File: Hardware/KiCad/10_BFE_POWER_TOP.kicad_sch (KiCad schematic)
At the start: 0 parts

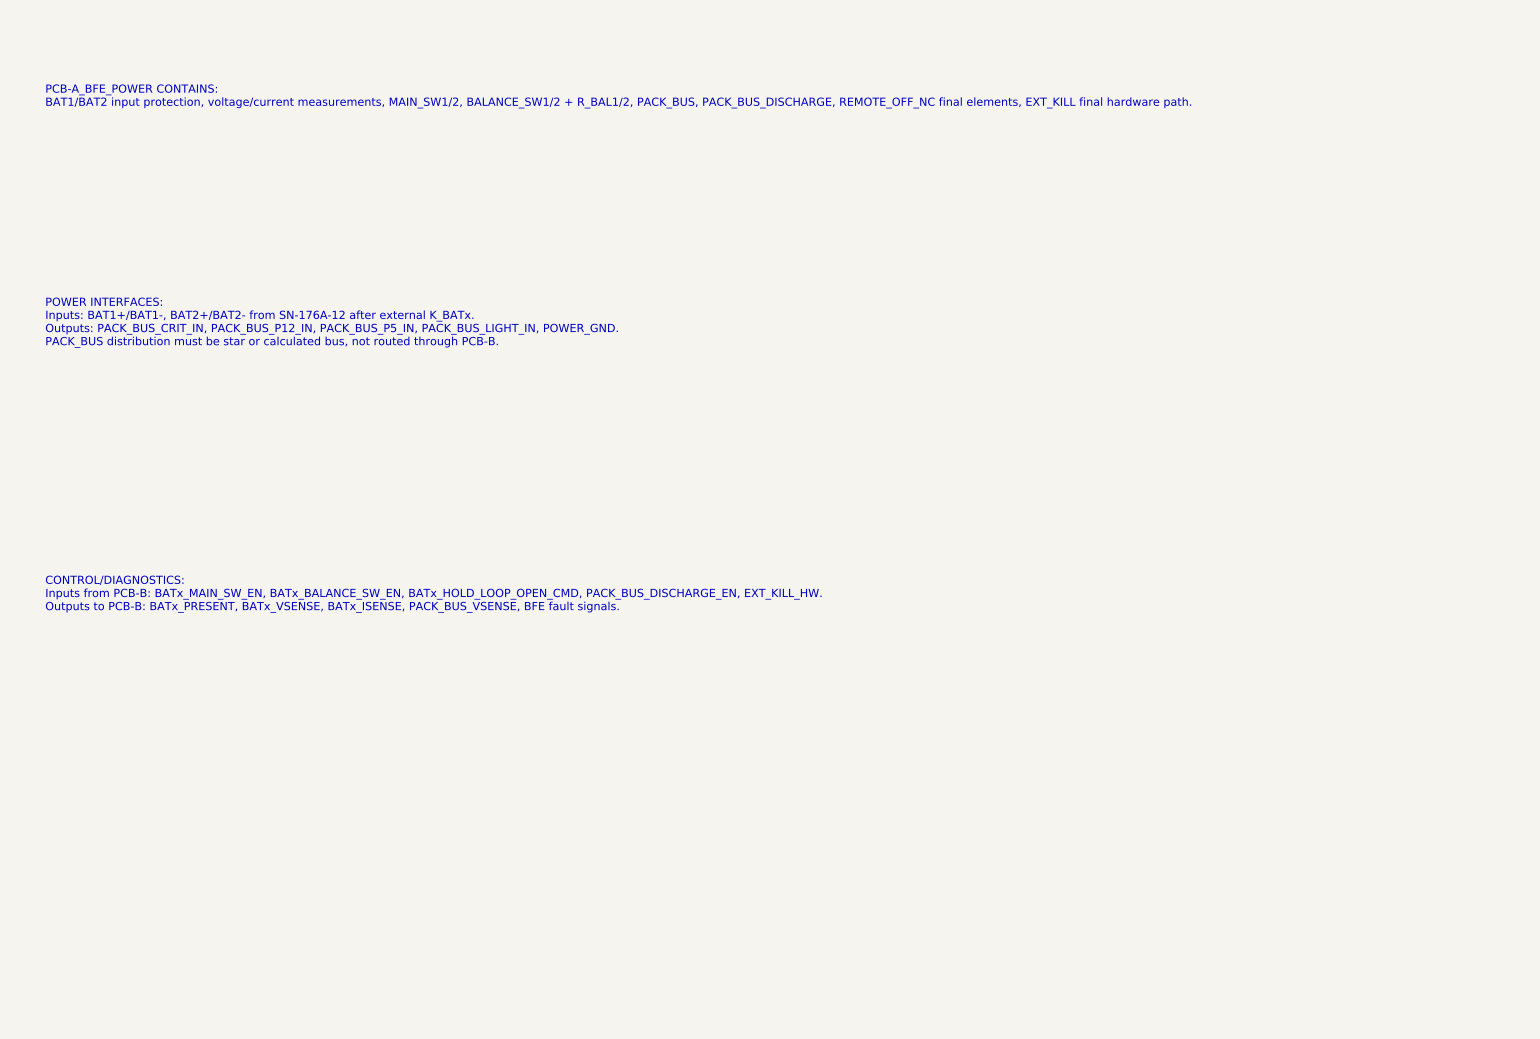
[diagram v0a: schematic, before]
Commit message: hardware: detail 10 BFE power top sheet
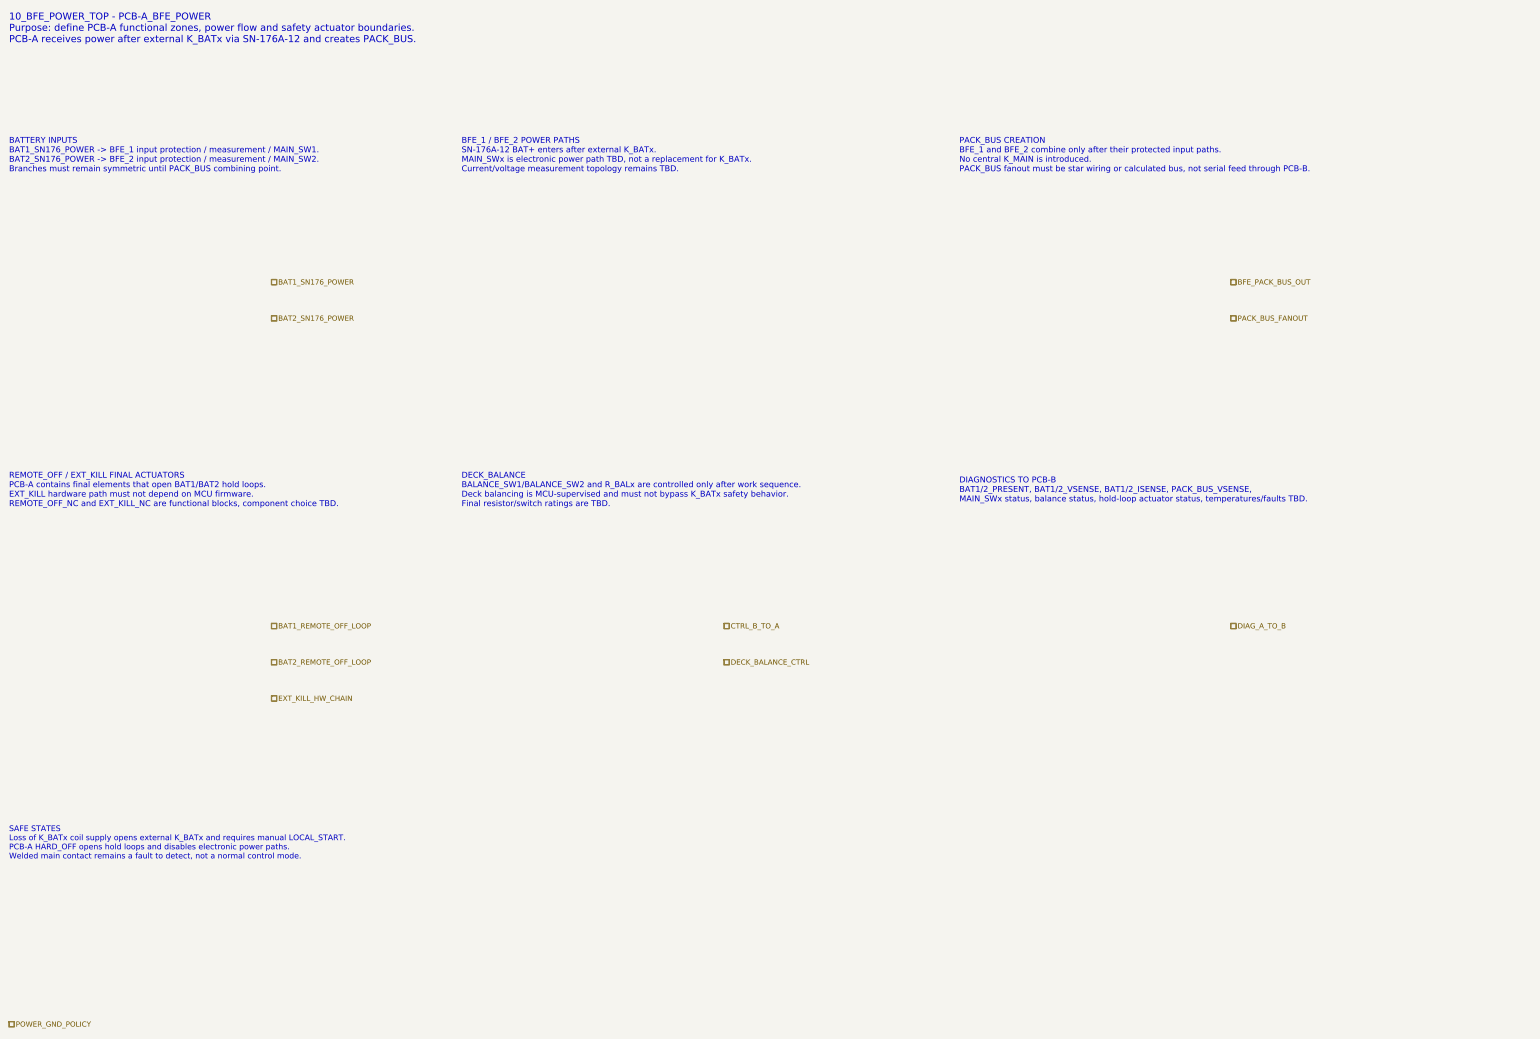
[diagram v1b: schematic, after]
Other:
- note added: "10_BFE_POWER_TOP - PCB-A_BFE_POWER Purpose: define PCB-A functional zones, power flow and safety actuator boundaries. PCB-A receives power after external K_BATx via SN-176A-12 and creates PACK_BUS."
- note added: "BATTERY INPUTS BAT1_SN176_POWER -> BFE_1 input protection / measurement / MAIN_SW1. BAT2_SN176_POWER -> BFE_2 input protection / measurement / MAIN_SW2. Branches must remain symmetric until PACK_BUS combining point."
- note added: "BFE_1 / BFE_2 POWER PATHS SN-176A-12 BAT+ enters after external K_BATx. MAIN_SWx is electronic power path TBD, not a replacement for K_BATx. Current/voltage measurement topology remains TBD."
- note added: "DECK_BALANCE BALANCE_SW1/BALANCE_SW2 and R_BALx are controlled only after work sequence. Deck balancing is MCU-supervised and must not bypass K_BATx safety behavior. Final resistor/switch ratings are TBD."
- note added: "DIAGNOSTICS TO PCB-B BAT1/2_PRESENT, BAT1/2_VSENSE, BAT1/2_ISENSE, PACK_BUS_VSENSE, MAIN_SWx status, balance status, hold-loop actuator status, temperatures/faults TBD."
- note added: "PACK_BUS CREATION BFE_1 and BFE_2 combine only after their protected input paths. No central K_MAIN is introduced. PACK_BUS fanout must be star wiring or calculated bus, not serial feed through PCB-B."
- note added: "REMOTE_OFF / EXT_KILL FINAL ACTUATORS PCB-A contains final elements that open BAT1/BAT2 hold loops. EXT_KILL hardware path must not depend on MCU firmware. REMOTE_OFF_NC and EXT_KILL_NC are functional blocks, component choice TBD."
- note added: "SAFE STATES Loss of K_BATx coil supply opens external K_BATx and requires manual LOCAL_START. PCB-A HARD_OFF opens hold loops and disables electronic power paths. Welded main contact remains a fault to detect, not a normal control mode."
- note removed: "CONTROL/DIAGNOSTICS: Inputs from PCB-B: BATx_MAIN_SW_EN, BATx_BALANCE_SW_EN, BATx_HOLD_LOOP_OPEN_CMD, PACK_BUS_DISCHARGE_EN, EXT_KILL_HW. Outputs to PCB-B: BATx_PRESENT, BATx_VSENSE, BATx_ISENSE, PACK_BUS_VSENSE, BFE fault signals."
- note removed: "PCB-A_BFE_POWER CONTAINS: BAT1/BAT2 input protection, voltage/current measurements, MAIN_SW1/2, BALANCE_SW1/2 + R_BAL1/2, PACK_BUS, PACK_BUS_DISCHARGE, REMOTE_OFF_NC final elements, EXT_KILL final hardware path."
- note removed: "POWER INTERFACES: Inputs: BAT1+/BAT1-, BAT2+/BAT2- from SN-176A-12 after external K_BATx. Outputs: PACK_BUS_CRIT_IN, PACK_BUS_P12_IN, PACK_BUS_P5_IN, PACK_BUS_LIGHT_IN, POWER_GND. PACK_BUS distribution must be star or calculated bus, not routed through PCB-B."
- company: (none) -> Gonoboben/plataVM
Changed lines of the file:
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@@
 	(title_block
 		(title "10_BFE_POWER_TOP - PCB-A_BFE_POWER")
-		(date "2026-07-14")
-		(rev "A0")
-		(comment 1 "Battery Front-End, PACK_BUS, DECK_BALANCE, HARD_OFF final actuators")
+		(date "2026-07-15")
+		(rev "A1")
+		(company "Gonoboben/plataVM")
+		(comment 1 "Architecture Level A: BFE branches, PACK_BUS and final HARD_OFF actuators")
+		(comment 2 "No K_BATx/MAIN_SWx/current sensor part numbers selected")
 	)
-	(text "POWER INTERFACES:\nInputs: BAT1+/BAT1-, BAT2+/BAT2- from SN-176A-12 after external K_BATx.\nOutputs: PACK_BUS_CRIT_IN, PACK_BUS_P12_IN, PACK_BUS_P5_IN, PACK_BUS_LIGHT_IN, POWER_GND.\nPACK_BUS distribution must be star or calculated bus, not routed through PCB-B."
+	(text "10_BFE_POWER_TOP - PCB-A_BFE_POWER\nPurpose: define PCB-A functional zones, power flow and safety actuator boundaries.\nPCB-A receives power after external K_BATx via SN-176A-12 and creates PACK_BUS."
 		(exclude_from_sim no)
-		(at 20 75 0)
-		(effects
-			(font
-				(size 1.8 1.8)
-			)
-			(justify left)
-		)
+		(at 12 10 0)
+		(effects (font (size 1.55 1.55)) (justify left))
+		(uuid "bfe-a-text-0001")
 	)
-	(text "CONTROL/DIAGNOSTICS:\nInputs from PCB-B: BATx_MAIN_SW_EN, BATx_BALANCE_SW_EN, BATx_HOLD_LOOP_OPEN_CMD, PACK_BUS_DISCHARGE_EN, EXT_KILL_HW.\nOutputs to PCB-B: BATx_PRESENT, BATx_VSENSE, BATx_ISENSE, PACK_BUS_VSENSE, BFE fault signals."
+	(text "BATTERY INPUTS\nBAT1_SN176_POWER -> BFE_1 input protection / measurement / MAIN_SW1.\nBAT2_SN176_POWER -> BFE_2 input protection / measurement / MAIN_SW2.\nBranches must remain symmetric until PACK_BUS combining point."
 		(exclude_from_sim no)
-		(at 20 135 0)
-		(effects
-			(font
-				(size 1.8 1.8)
-			)
-			(justify left)
-		)
+		(at 12 38 0)
+		(effects (font (size 1.3 1.3)) (justify left))
+		(uuid "bfe-a-text-0002")
 	)
-	(text "PCB-A_BFE_POWER CONTAINS:\nBAT1/BAT2 input protection, voltage/current measurements, MAIN_SW1/2, BALANCE_SW1/2 + R_BAL1/2, PACK_BUS, PACK_BUS_DISCHARGE, REMOTE_OFF_NC final elements, EXT_KILL final hardware path."
+	(text "BFE_1 / BFE_2 POWER PATHS\nSN-176A-12 BAT+ enters after external K_BATx.\nMAIN_SWx is electronic power path TBD, not a replacement for K_BATx.\nCurrent/voltage measurement topology remains TBD."
 		(exclude_from_sim no)
-		(at 20 25 0)
-		(effects
-			(font
-				(size 1.8 1.8)
-			)
-			(justify left)
-		)
+		(at 112 38 0)
+		(effects (font (size 1.3 1.3)) (justify left))
+		(uuid "bfe-a-text-0003")
 	)
+	(text "PACK_BUS CREATION\nBFE_1 and BFE_2 combine only after their protected input paths.\nNo central K_MAIN is introduced.\nPACK_BUS fanout must be star wiring or calculated bus, not serial feed through PCB-B."
+		(exclude_from_sim no)
+		(at 222 38 0)
+		(effects (font (size 1.3 1.3)) (justify left))
+		(uuid "bfe-a-text-0004")
+	)
+	(text "REMOTE_OFF / EXT_KILL FINAL ACTUATORS\nPCB-A contains final elements that open BAT1/BAT2 hold loops.\nEXT_KILL hardware path must not depend on MCU firmware.\nREMOTE_OFF_NC and EXT_KILL_NC are functional blocks, component choice TBD."
+		(exclude_from_sim no)
+		(at 12 112 0)
+		(effects (font (size 1.3 1.3)) (justify left))
+		(uuid "bfe-a-text-0005")
+	)
+	(text "DECK_BALANCE\nBALANCE_SW1/BALANCE_SW2 and R_BALx are controlled only after work sequence.\nDeck balancing is MCU-supervised and must not bypass K_BATx safety behavior.\nFinal resistor/switch ratings are TBD."
+		(exclude_from_sim no)
+		(at 112 112 0)
+		(effects (font (size 1.3 1.3)) (justify left))
+		(uuid "bfe-a-text-0006")
+	)
+	(text "DIAGNOSTICS TO PCB-B\nBAT1/2_PRESENT, BAT1/2_VSENSE, BAT1/2_ISENSE, PACK_BUS_VSENSE,\nMAIN_SWx status, balance status, hold-loop actuator status, temperatures/faults TBD."
+		(exclude_from_sim no)
+		(at 222 112 0)
+		(effects (font (size 1.3 1.3)) (justify left))
+		(uuid "bfe-a-text-0007")
+	)
+	(text "SAFE STATES\nLoss of K_BATx coil supply opens external K_BATx and requires manual LOCAL_START.\nPCB-A HARD_OFF opens hold loops and disables electronic power paths.\nWelded main contact remains a fault to detect, not a normal control mode."
+		(exclude_from_sim no)
+		(at 12 190 0)
+		(effects (font (size 1.25 1.25)) (justify left))
+		(uuid "bfe-a-text-0008")
+	)
+	(hierarchical_label "BAT1_SN176_POWER" (shape passive) (exclude_from_sim no) (at 70 66 0) (effects (font (size 1.15 1.15)) (justify left)) (uuid "bfe-a-label-0001"))
+	(hierarchical_label "BAT2_SN176_POWER" (shape passive) (exclude_from_sim no) (at 70 74 0) (effects (font (size 1.15 1.15)) (justify left)) (uuid "bfe-a-label-0002"))
+	(hierarchical_label "BAT1_REMOTE_OFF_LOOP" (shape passive) (exclude_from_sim no) (at 70 142 0) (effects (font (size 1.15 1.15)) (justify left)) (uuid "bfe-a-label-0003"))
+	(hierarchical_label "BAT2_REMOTE_OFF_LOOP" (shape passive) (exclude_from_sim no) (at 70 150 0) (effects (font (size 1.15 1.15)) (justify left)) (uuid "bfe-a-label-0004"))
+	(hierarchical_label "EXT_KILL_HW_CHAIN" (shape passive) (exclude_from_sim no) (at 70 158 0) (effects (font (size 1.15 1.15)) (justify left)) (uuid "bfe-a-label-0005"))
+	(hierarchical_label "BFE_PACK_BUS_OUT" (shape passive) (exclude_from_sim no) (at 282 66 0) (effects (font (size 1.15 1.15)) (justify left)) (uuid "bfe-a-label-0006"))
+	(hierarchical_label "PACK_BUS_FANOUT" (shape passive) (exclude_from_sim no) (at 282 74 0) (effects (font (size 1.15 1.15)) (justify left)) (uuid "bfe-a-label-0007"))
+	(hierarchical_label "CTRL_B_TO_A" (shape passive) (exclude_from_sim no) (at 170 142 0) (effects (font (size 1.15 1.15)) (justify left)) (uuid "bfe-a-label-0008"))
+	(hierarchical_label "DIAG_A_TO_B" (shape passive) (exclude_from_sim no) (at 282 142 0) (effects (font (size 1.15 1.15)) (justify left)) (uuid "bfe-a-label-0009"))
+	(hierarchical_label "DECK_BALANCE_CTRL" (shape passive) (exclude_from_sim no) (at 170 150 0) (effects (font (size 1.15 1.15)) (justify left)) (uuid "bfe-a-label-0010"))
+	(hierarchical_label "POWER_GND_POLICY" (shape passive) (exclude_from_sim no) (at 12 230 0) (effects (font (size 1.15 1.15)) (justify left)) (uuid "bfe-a-label-0011"))
 )
